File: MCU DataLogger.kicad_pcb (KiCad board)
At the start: 2 copper layers, 0 parts

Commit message: Setup Pcbnew.
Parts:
- added BT1: Battery, Connector_PinHeader_2.54mm:PinHeader_1x02_P2.54mm_Vertical, F.Cu at (139.7, 101.6)
- added C1: 0.1uF, Capacitor_SMD:C_0805_2012Metric, F.Cu at (154.7, 94.2)
- added C2: 22pF, Capacitor_SMD:C_0805_2012Metric, F.Cu at (129.2, 101.0)
- added C3: 22pF, Capacitor_SMD:C_0805_2012Metric, F.Cu at (133.2, 114.2)
- added C4: 0.1uF, Capacitor_SMD:C_0805_2012Metric, F.Cu at (137.7, 113.7)
- added C5: 100nF, Capacitor_SMD:C_0805_2012Metric, F.Cu at (133.7, 101.0)
- added D1: LED, LED_SMD:LED_0805_2012Metric, F.Cu at (150.0, 100.0)
- added D2: LED, LED_SMD:LED_0805_2012Metric, F.Cu at (133.2, 111.1)
- added H1: MountingHole, MountingHole:MountingHole_2.1mm, F.Cu at (149.6, 95.6)
- added H2: MountingHole, MountingHole:MountingHole_2.1mm, F.Cu at (144.9, 102.2)
- added H3: MountingHole, MountingHole:MountingHole_2.1mm, F.Cu at (138.4, 109.3)
- added H4: MountingHole, MountingHole:MountingHole_2.1mm, F.Cu at (128.1, 114.4)
- added J1: Conn_01x04_Male, Connector_PinHeader_2.54mm:PinHeader_1x04_P2.54mm_Vertical, F.Cu at (170.1, 95.0)
- added J2: Conn_01x04_Male, Connector_PinHeader_2.54mm:PinHeader_1x04_P2.54mm_Vertical, F.Cu at (174.8, 95.0)
- added J3: Conn_01x09_Male, Connector_PinHeader_2.54mm:PinHeader_1x09_P2.54mm_Vertical, F.Cu at (165.5, 95.0)
- added J4: Conn_02x03_Odd_Even, Connector_PinHeader_2.54mm:PinHeader_2x03_P2.54mm_Vertical, F.Cu at (179.4, 95.0)
- added R1: 4.7K, Resistor_SMD:R_0805_2012Metric, F.Cu at (150.0, 103.0)
- added R2: 4.7K, Resistor_SMD:R_0805_2012Metric, F.Cu at (154.4, 100.2)
- added R3: 10K, Resistor_SMD:R_0805_2012Metric, F.Cu at (143.5, 109.5)
- added R4: 10K, Resistor_SMD:R_0805_2012Metric, F.Cu at (148.6, 106.5)
- added R5: 330, Resistor_SMD:R_0805_2012Metric, F.Cu at (142.1, 113.7)
- added R6: 10K, Resistor_SMD:R_0805_2012Metric, F.Cu at (144.2, 106.5)
- added R7: 330, Resistor_SMD:R_0805_2012Metric, F.Cu at (154.7, 97.2)
- added U1: 24LC1025, Package_SO:SOIC-8_5.23x5.23mm_P1.27mm, F.Cu at (132.2, 96.1)
- added U2: 24LC1025, Package_SO:SOIC-8_5.23x5.23mm_P1.27mm, F.Cu at (120.2, 108.2)
- added U3: DS1337S+, Libraries:SOIC127P600X175-8N, F.Cu at (142.5, 96.0)
- added U4: ATMEGA328P-AU, Libraries:QFP80P900X900X120-32N, F.Cu at (121.0, 98.8)
- added Y1: 32.768 KHz, Crystal:Crystal_SMD_5032-2Pin_5.0x3.2mm_HandSoldering, F.Cu at (130.4, 107.2)
- added Y2: 16 MHz, Crystal:Crystal_SMD_5032-2Pin_5.0x3.2mm_HandSoldering, F.Cu at (120.1, 114.0)

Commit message: Completed footprints.
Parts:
- moved J3 121.4 mm to (45.1, 111.1), turned to 90 degrees
- moved H1 109.4 mm to (40.6, 86.4)
- moved J2 105.5 mm to (70.5, 111.1), turned to 90 degrees
- moved H2 104.7 mm to (40.6, 111.8)
- moved BT1 97.6 mm to (42.5, 92.7)
- moved J4 97.0 mm to (82.5, 90.8)
- moved C1 96.7 mm to (58.4, 85.7)
- moved R4 96.6 mm to (52.1, 107.3), turned to 180 degrees
- moved R3 95.6 mm to (48.0, 107.3)
- moved U3 92.6 mm to (50.2, 102.2)
- moved Y1 88.0 mm to (42.5, 103.5), turned to 90 degrees
- moved J1 85.2 mm to (85.1, 99.7)
- moved R7 82.1 mm to (73.0, 88.9)
- moved U1 82.0 mm to (50.2, 94.6)
- moved R2 81.7 mm to (73.1, 92.1), turned to 180 degrees
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
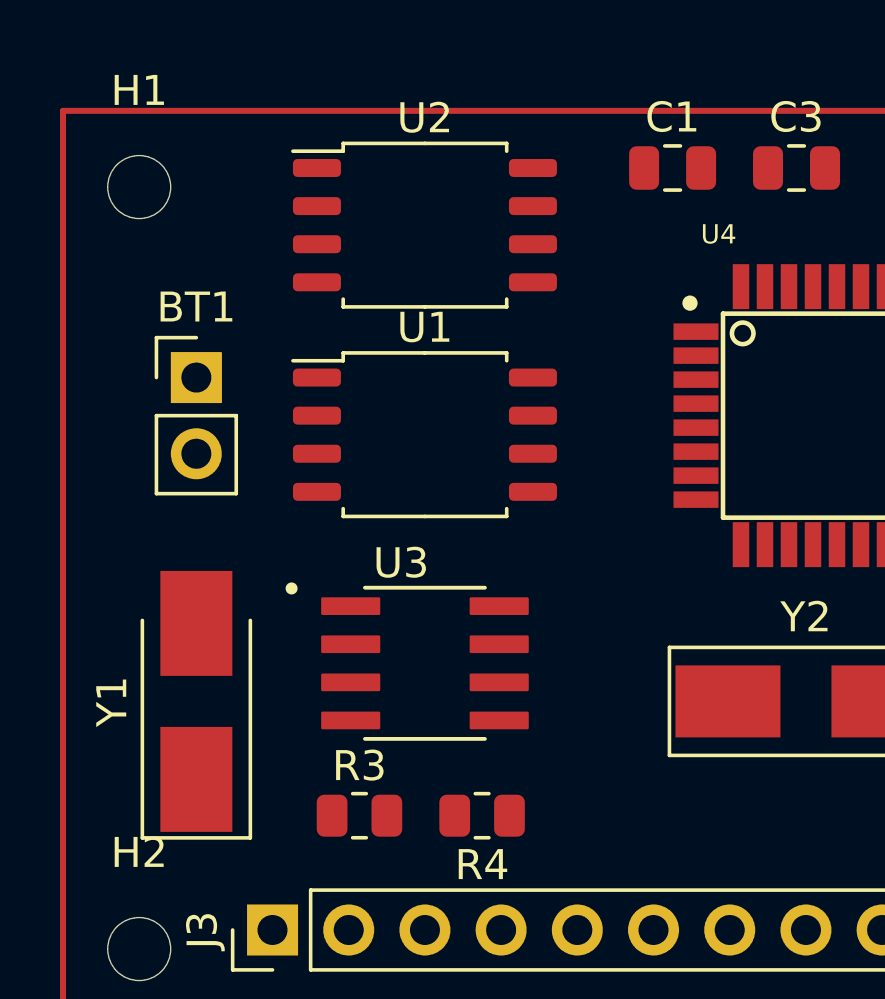
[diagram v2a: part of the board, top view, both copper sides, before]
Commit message: First routes.
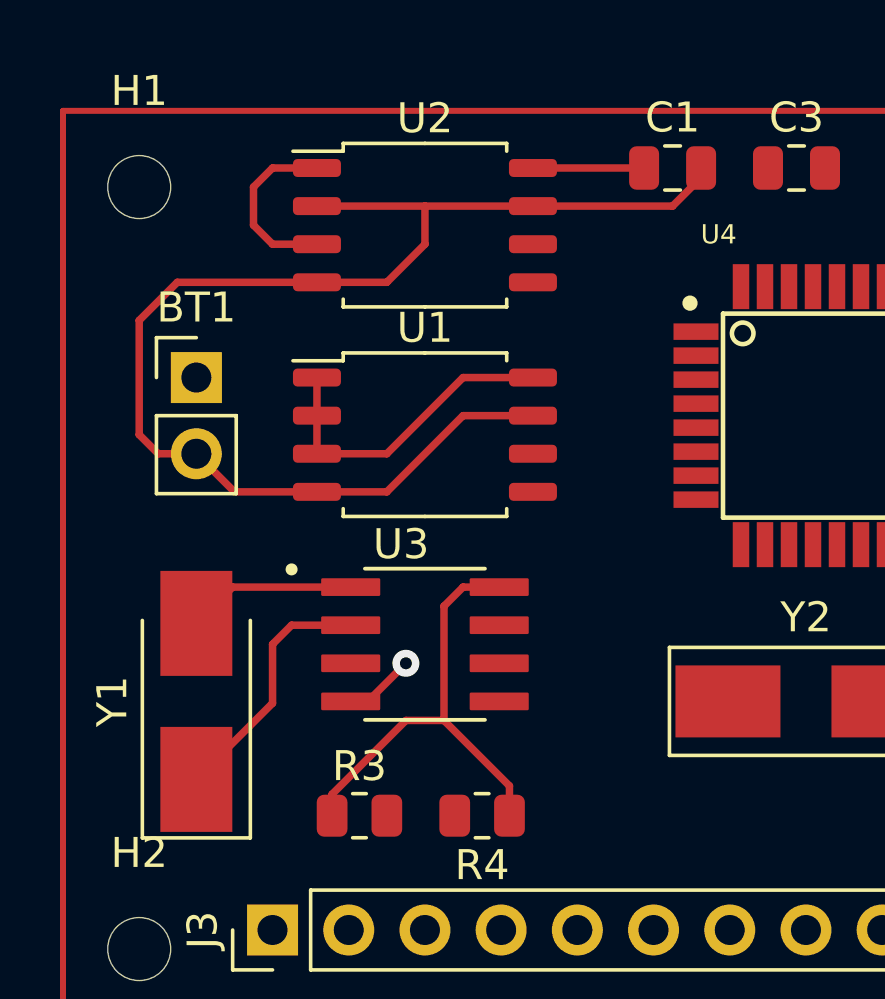
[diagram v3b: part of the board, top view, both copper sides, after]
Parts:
- moved U3 0.64 mm to (50.2, 101.6)
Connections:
- C1 pad 1: Net-(C1-Pad1) -> /Vcc
- R3 pad 1: Net-(C1-Pad1) -> /Vcc
- R4 pad 1: Net-(C1-Pad1) -> /Vcc
- U3 pad 8: Net-(C1-Pad1) -> /Vcc
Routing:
- net GND: track 0.00 -> 46.5 mm, vias 0 -> 1
- net /Vcc: track 0.00 -> 36.0 mm
- net Net-(U3-Pad2): track 0.00 -> 8.98 mm
- net Net-(U3-Pad1): track 0.00 -> 5.65 mm

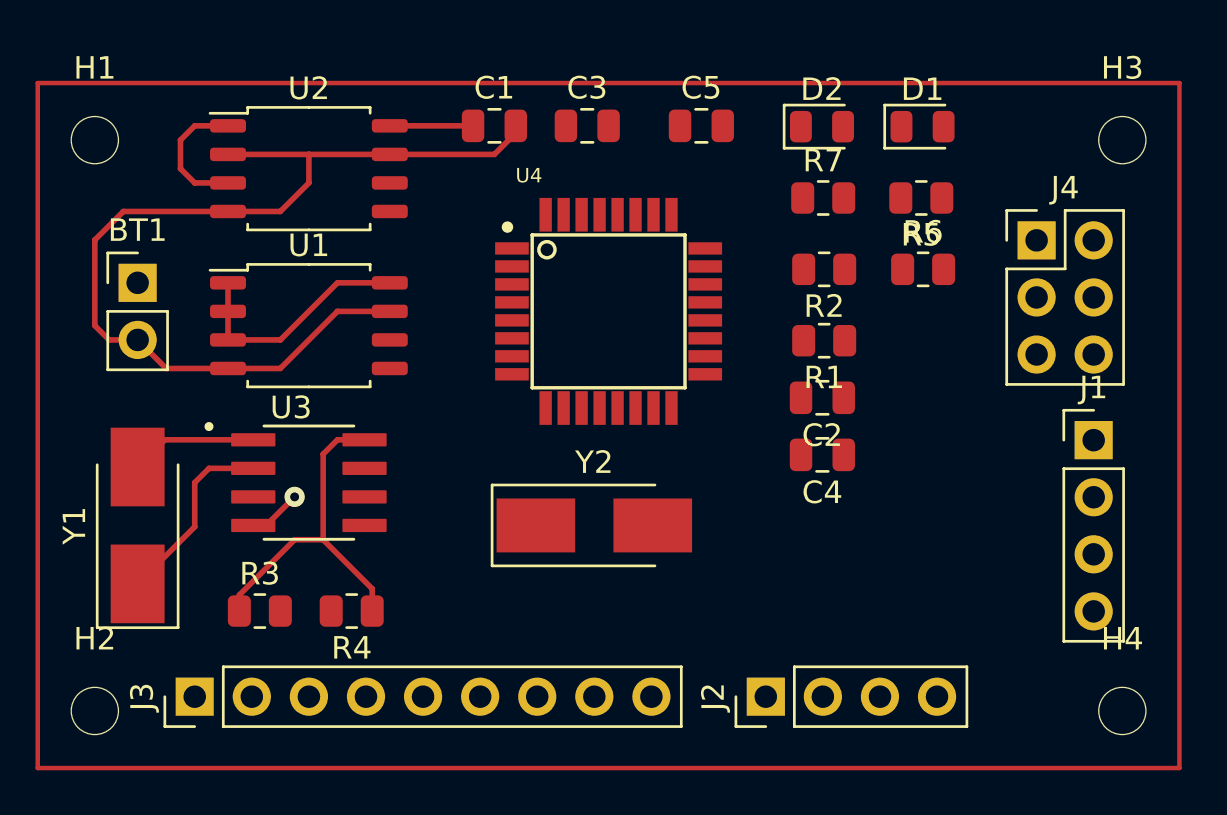
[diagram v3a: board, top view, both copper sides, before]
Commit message: Routing sans GND Vcc complete.
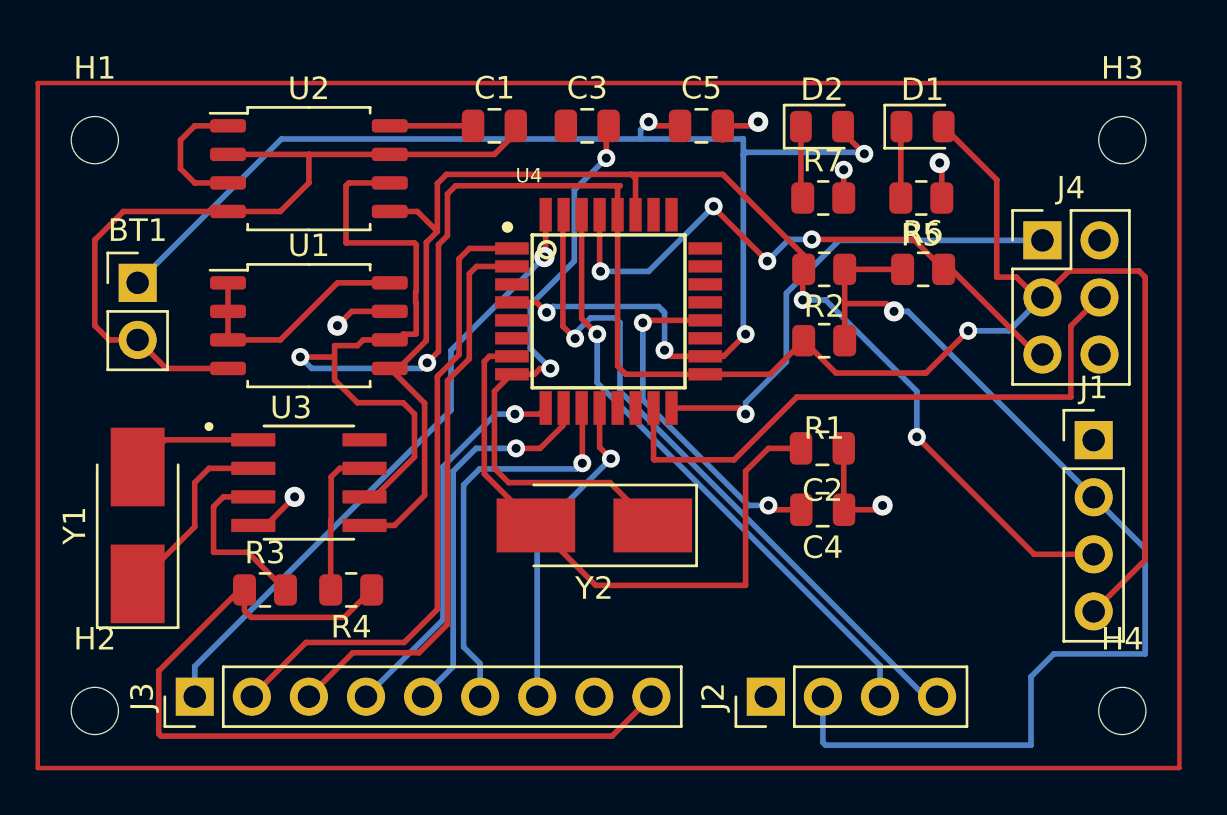
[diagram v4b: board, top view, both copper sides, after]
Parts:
- moved C4 2.44 mm to (73.0, 102.8)
- moved C2 2.25 mm to (73.0, 100.1)
- moved R3 0.97 mm to (48.2, 106.4)
- moved R4 0.94 mm to (52.0, 106.4)
- moved J4 0.26 mm to (82.8, 90.8)
- turned Y2 to 180 degrees
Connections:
- C2 pad 1: Net-(C2-Pad1) -> GND
- C2 pad 2: GND -> Net-(U4-Pad7)
- J4 pad 1: /MOSI -> /MISO
- J4 pad 4: /MISO -> /MOSI
- U4 pad 7: Net-(C2-Pad1) -> Net-(U4-Pad7)
- Y2 pad 2: Net-(C2-Pad1) -> Net-(U4-Pad7)
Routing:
- net /SCK: track 0.00 -> 109.9 mm, vias 0 -> 3
- net /Vcc: track 36.0 -> 106.7 mm, vias 0 -> 1
- net /SDA: track 0.00 -> 62.0 mm, vias 0 -> 2
- net Net-(BT1-Pad1): track 0.00 -> 60.8 mm, vias 0 -> 5
- net /TX: track 0.00 -> 31.1 mm, vias 0 -> 1
- net /D3: track 0.00 -> 28.4 mm
- net Net-(U4-Pad7): track 0.00 -> 28.0 mm
- net /D2: track 0.00 -> 27.9 mm, vias 0 -> 1
- net Net-(C3-Pad2): track 0.00 -> 27.0 mm, vias 0 -> 2
- net /MOSI: track 0.00 -> 27.0 mm
- net /RX: track 0.00 -> 26.9 mm, vias 0 -> 1
- net /RESET: track 0.00 -> 26.7 mm, vias 0 -> 4
- net /D4: track 0.00 -> 25.5 mm
- net /MISO: track 0.00 -> 21.9 mm, vias 0 -> 1
- net /D7: track 0.00 -> 17.9 mm, vias 0 -> 1
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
